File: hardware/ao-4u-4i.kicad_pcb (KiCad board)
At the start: 4 copper layers, 100 x 85 mm, 225 parts, among them J101 TNG-Power-TOP, J102 TNG-Power-BTM, J103 TNG-Data-TOP, J104 TNG-Data-BTM, P102 Debug, P103 PE, P201 INPUT0, P202 INPUT1, P203 INPUT2, P204 INPUT3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

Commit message: fix tbd
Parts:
- C108, C109: value TBD -> 33pF
- X101: value TBD -> 8MHz

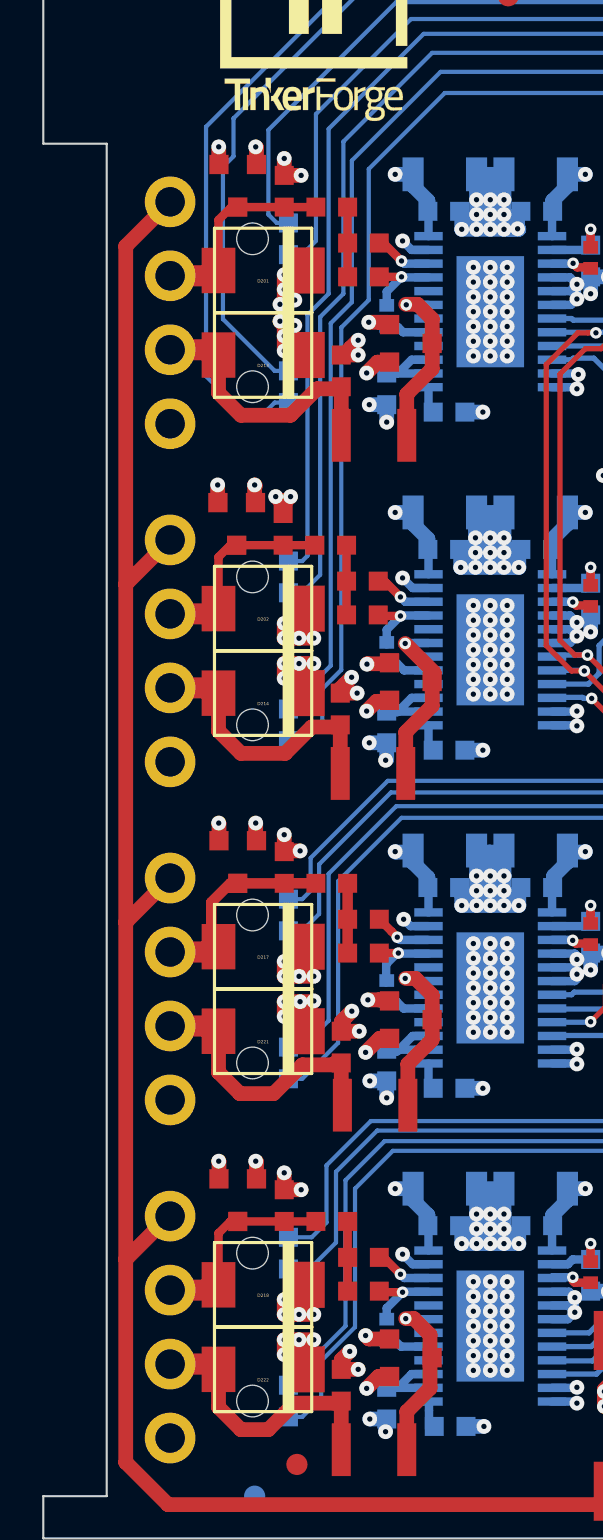
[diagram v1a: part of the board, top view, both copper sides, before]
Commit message: fix diode orientation
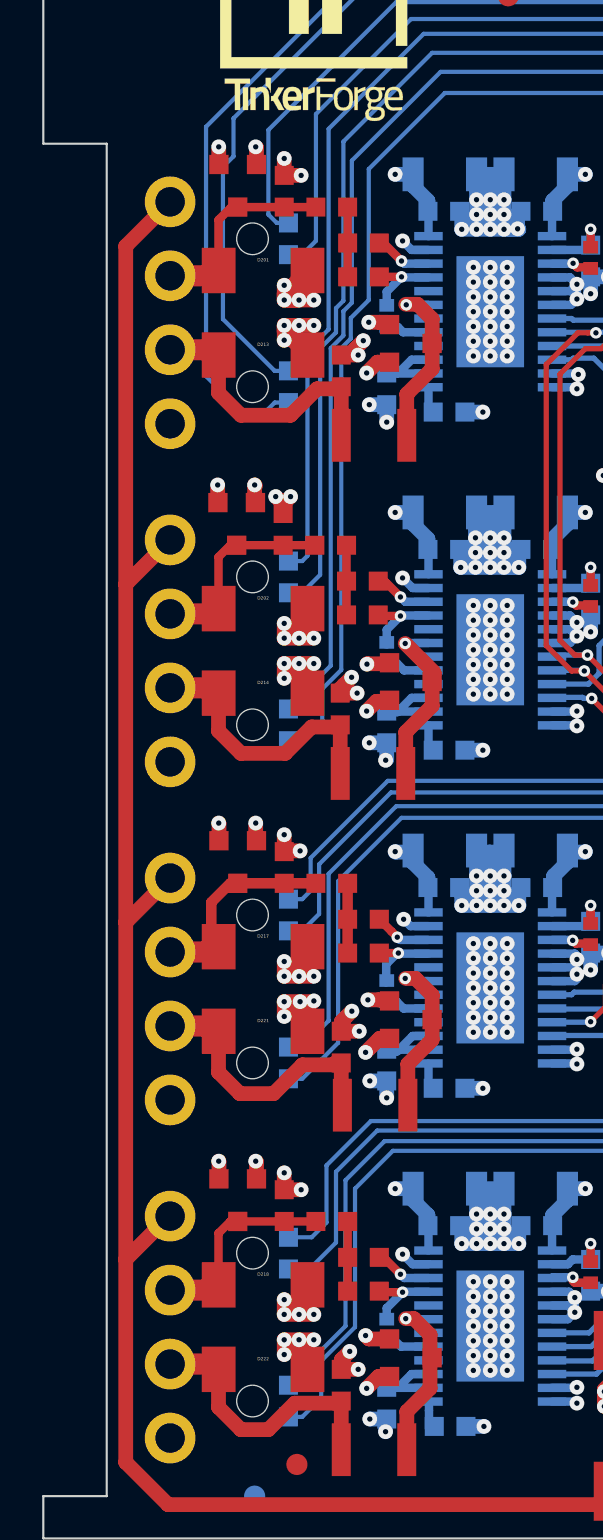
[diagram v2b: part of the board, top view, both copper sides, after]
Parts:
- turned D201 to 180 degrees
- turned D202 to 180 degrees
- turned D213 to 180 degrees
- turned D214 to 180 degrees
- turned D217 to 180 degrees
- turned D218 to 180 degrees
- turned D221 to 180 degrees
- turned D222 to 180 degrees
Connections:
- D201 pad 1: Net-(C201-Pad2) -> AGND
- D201 pad 2: AGND -> Net-(C201-Pad2)
- D202 pad 1: Net-(C202-Pad2) -> AGND
- D202 pad 2: AGND -> Net-(C202-Pad2)
- D213 pad 1: Net-(C203-Pad2) -> AGND
- D213 pad 2: AGND -> Net-(C203-Pad2)
- D214 pad 1: Net-(C204-Pad2) -> AGND
- D214 pad 2: AGND -> Net-(C204-Pad2)
- D217 pad 1: Net-(C219-Pad2) -> AGND
- D217 pad 2: AGND -> Net-(C219-Pad2)
- D218 pad 1: Net-(C220-Pad2) -> AGND
- D218 pad 2: AGND -> Net-(C220-Pad2)
- D221 pad 1: Net-(C221-Pad2) -> AGND
- D221 pad 2: AGND -> Net-(C221-Pad2)
- D222 pad 1: Net-(C222-Pad2) -> AGND
- D222 pad 2: AGND -> Net-(C222-Pad2)
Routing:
- net AGND: track 310.2 -> 311.9 mm

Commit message: specify capacitors
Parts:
- C113, C114: value TBD/47pF -> 47pF

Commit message: fix stuff
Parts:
- C110: footprint C0805 -> kicad-libraries:C0805E
- C250: footprint kicad-libraries:C0805 -> kicad-libraries:C0805E
- P201: value INPUT0 -> OUTPUT0
- P202: value INPUT1 -> OUTPUT1
- P203: value INPUT2 -> OUTPUT2
- P204: value INPUT3 -> OUTPUT3
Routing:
- net AGND: track 311.9 -> 311.2 mm, vias 271 -> 270

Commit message: fix values
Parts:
- C111, C122, C123, C124: value 100µF/35V -> 100uF/35V
- C118: value 10µF/50V -> 10uF/50V
- C121, C125, C126: value 10µF/35V -> 10uF/35V
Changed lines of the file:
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@@
       (effects (font (size 0.3 0.3) (thickness 0.075)))
     )
-    (fp_text value 10µF/50V (at 0 -0.65 -180) (layer F.Fab)
+    (fp_text value 10uF/50V (at 0 -0.65 -180) (layer F.Fab)
       (effects (font (size 0.3 0.3) (thickness 0.075)))
     )
@@
       (effects (font (size 0.3 0.3) (thickness 0.075)) (justify mirror))
     )
-    (fp_text value 10µF/35V (at 0 0.65 90) (layer B.Fab)
+    (fp_text value 10uF/35V (at 0 0.65 90) (layer B.Fab)
       (effects (font (size 0.3 0.3) (thickness 0.075)) (justify mirror))
     )
@@
       (effects (font (size 0.3 0.3) (thickness 0.075)))
     )
-    (fp_text value 10µF/35V (at 0 -0.65) (layer F.Fab)
+    (fp_text value 10uF/35V (at 0 -0.65) (layer F.Fab)
       (effects (font (size 0.3 0.3) (thickness 0.075)))
     )
@@
       (effects (font (size 0.3 0.3) (thickness 0.075)))
     )
-    (fp_text value 10µF/35V (at 0 -0.65) (layer F.Fab)
+    (fp_text value 10uF/35V (at 0 -0.65) (layer F.Fab)
       (effects (font (size 0.3 0.3) (thickness 0.075)))
     )
@@
       (effects (font (size 0.59944 0.59944) (thickness 0.12446)))
     )
-    (fp_text value 100µF/35V (at 0.95 -0.375) (layer F.Fab)
+    (fp_text value 100uF/35V (at 0.95 -0.375) (layer F.Fab)
       (effects (font (size 0.59944 0.59944) (thickness 0.12446)))
     )
@@
       (effects (font (size 0.59944 0.59944) (thickness 0.12446)))
     )
-    (fp_text value 100µF/35V (at 0.95 -0.375 90) (layer F.Fab)
+    (fp_text value 100uF/35V (at 0.95 -0.375 90) (layer F.Fab)
       (effects (font (size 0.59944 0.59944) (thickness 0.12446)))
     )
@@
       (effects (font (size 0.59944 0.59944) (thickness 0.12446)))
     )
-    (fp_text value 100µF/35V (at 0.95 -0.375) (layer F.Fab)
+    (fp_text value 100uF/35V (at 0.95 -0.375) (layer F.Fab)
       (effects (font (size 0.59944 0.59944) (thickness 0.12446)))
     )
@@
       (effects (font (size 0.59944 0.59944) (thickness 0.12446)))
     )
-    (fp_text value 100µF/35V (at 0.95 -0.375 90) (layer F.Fab)
+    (fp_text value 100uF/35V (at 0.95 -0.375 90) (layer F.Fab)
       (effects (font (size 0.59944 0.59944) (thickness 0.12446)))
     )

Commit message: improve routing
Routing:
- net -15V: track 302.5 -> 301.6 mm

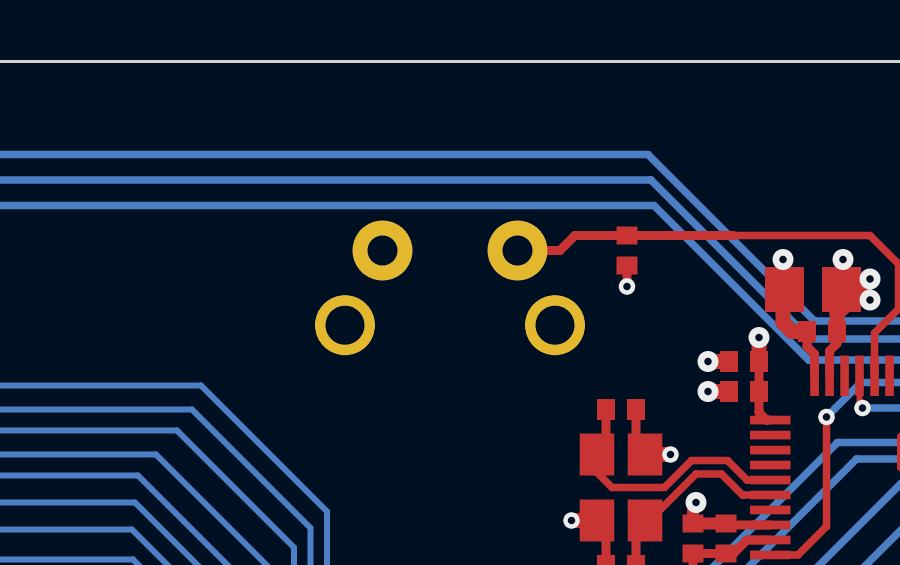
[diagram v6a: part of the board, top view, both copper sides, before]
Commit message: all footprints updated
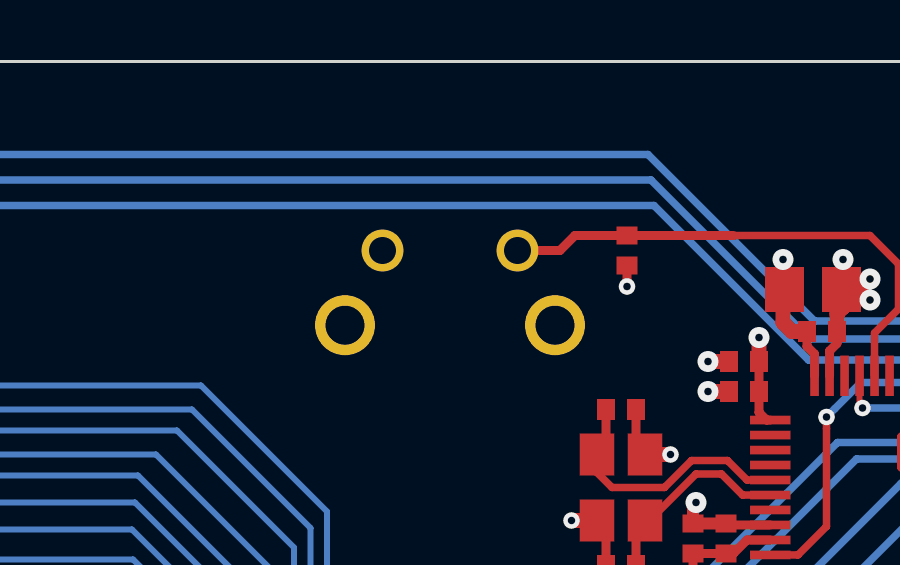
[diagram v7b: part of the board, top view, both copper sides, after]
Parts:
- C101, C102, C103, C104, C105, C106, C107, C108, C109, C112, C113, C114, C116, C117: footprint C0402F -> kicad-libraries:C0402F
- C115: footprint C0603F -> kicad-libraries:C0603F
- C118, C119, C120, C121, C125, C126, C127, C128: footprint C1206 -> kicad-libraries:C1206
- D203, D204, D205, D206, D207, D208, D209, D210: footprint LED-LP -> kicad-libraries:LED-LP
- J101, J103: footprint TNG-40-TOP -> kicad-libraries:TNG-40-TOP
- J102, J104: footprint TNG-40-BTM -> kicad-libraries:TNG-40-BTM
- L101, L102, L103, L104: footprint R0603F -> kicad-libraries:R0603F
- L105: footprint WE-CNSW-0603 -> kicad-libraries:WE-CNSW-0603
- LED101: footprint LED-RGB-LP -> kicad-libraries:LED-RGB-LP
- P201, P202, P203, P204: footprint OQ_4P -> kicad-libraries:OQ_4P
- R101, R102, R103, R104, R105, R106, R107, R108: footprint R0402F -> kicad-libraries:R0402F
- U103: footprint SOT563-SPEC -> kicad-libraries:SOT563-SPEC

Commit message: remove galvanic isolation as default
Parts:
- C101, C102, C103, C104, C105, C106, C107, C108, C109, C112, C113, C114, C116, C117: footprint kicad-libraries:C0402F -> C0402F
- C115: footprint kicad-libraries:C0603F -> C0603F
- C118, C121, C125, C126, C127, C128: footprint kicad-libraries:C1206 -> C1206
- C119, C120: value 1nF 2kV -> 0; footprint kicad-libraries:C1206 -> C1206
- D203, D204, D205, D206, D207, D208, D209, D210: footprint kicad-libraries:LED-LP -> LED-LP
- J101, J103: footprint kicad-libraries:TNG-40-TOP -> TNG-40-TOP
- J102, J104: footprint kicad-libraries:TNG-40-BTM -> TNG-40-BTM
- L101, L102, L103, L104: footprint kicad-libraries:R0603F -> R0603F
- L105: footprint kicad-libraries:WE-CNSW-0603 -> WE-CNSW-0603
- LED101: footprint kicad-libraries:LED-RGB-LP -> LED-RGB-LP
- P201, P202, P203, P204: footprint kicad-libraries:OQ_4P -> OQ_4P
- R101, R102, R103, R104, R105, R106, R107, R108: footprint kicad-libraries:R0402F -> R0402F
- U103: footprint kicad-libraries:SOT563-SPEC -> SOT563-SPEC
- U104: value TEL10 -> DNP
